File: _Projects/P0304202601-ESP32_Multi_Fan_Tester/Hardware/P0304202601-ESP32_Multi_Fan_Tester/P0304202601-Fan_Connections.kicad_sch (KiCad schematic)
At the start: 1 part, among them CN1 KHS4B-PH-SM4-TB(LF)(SN)

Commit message: Added new content from recent stream.
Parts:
- added CN4: KTBL002B-350-04GR-2OR, CONNECTORS:KTBTBL002B35004GR2OR, symbol CONNECTORS:KTBL002B-350-04GR-2OR
- added CN5: KH470533000, CONNECTORS:KH470533000, symbol CONNECTORS:KH470533000
- added J1, J2, J3: KH22-28-5021, CONNECTORS:2x1HDR2.54mm, symbol CONNECTORS:KH22-28-5021
- added R2: RC06031K0075AAA, COMPONENTS:RES-0603, symbol COMPONENTS:RC06031K0075AAA
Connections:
- new net +3.3V: R2.1
- new net FAN_PWM: CN5.4
- new net FAN_TACH: CN5.3, R2.2
- new net FAN_VCC: CN5.2
- new net GND: CN5.1
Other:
- moved on the sheet: CN1

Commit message: Added updated content that I keep forgetting to do.
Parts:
- added D3, D4, D5: DLQ62702P5179, COMPONENTS:LED-0805, symbol COMPONENTS:DLQ62702P5179
- added Q1, Q2, Q3: SSM3K2615R,LF, COMPONENTS:SOT-23F-3, symbol COMPONENTS:QSSM3K2615R,LF
- added R11: 100Ω, COMPONENTS:RES-0603, symbol COMPONENTS:RC0603100RAAD07500
- added R12: RC060310K2075AAA, COMPONENTS:RES-0603, symbol COMPONENTS:RC060310K2075AAA
- added R4: RC0603330075AAA, COMPONENTS:RES-0603, symbol COMPONENTS:RC0603330075AAA
- added R5: RC0603510075AAA, COMPONENTS:RES-0603, symbol COMPONENTS:RC0603510075AAA
- added R6: RC06031K0075AAA, COMPONENTS:RES-0603, symbol COMPONENTS:RC06031K0075AAA
- added TP3, TP4, TP5, TP6: TP5010, CONNECTORS:5010, symbol CONNECTORS:TP5010
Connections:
- net +12V: now also Q3.3 (D)
- net +3.3V: now also Q1.3 (D)
- net +5V: now also Q2.3 (D)
- net FAN_PWM: now also CN1.3, CN4.3, TP6.1
- net FAN_TACH: now also CN1.2, CN4.2, TP3.1
- net FAN_VCC: now also CN1.1, CN4.1, J1.2, J2.2, J3.2, R4.1, R5.1, R6.1
- net GND: now also CN1.4, CN4.4, D3.1 (K), D4.1 (K), D5.1 (K), R12.2, TP5.1
- net at J2.1: now also Q2.2 (S)
- net at J3.1: now also Q3.2 (S)
- net at J1.1: now also Q1.2 (S)
- new net: D5.2 (A), R6.2
- new net: D3.2 (A), R4.2
- new net: D4.2 (A), R5.2
- new net FAN_PWR_CNTROL: R11.1, R12.1, TP4.1
- new net PWR_CNTRL: Q1.1 (G), Q2.1 (G), Q3.1 (G), R11.2
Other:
- moved on the sheet: CN1, CN4, CN5, J1, J2, J3, R2

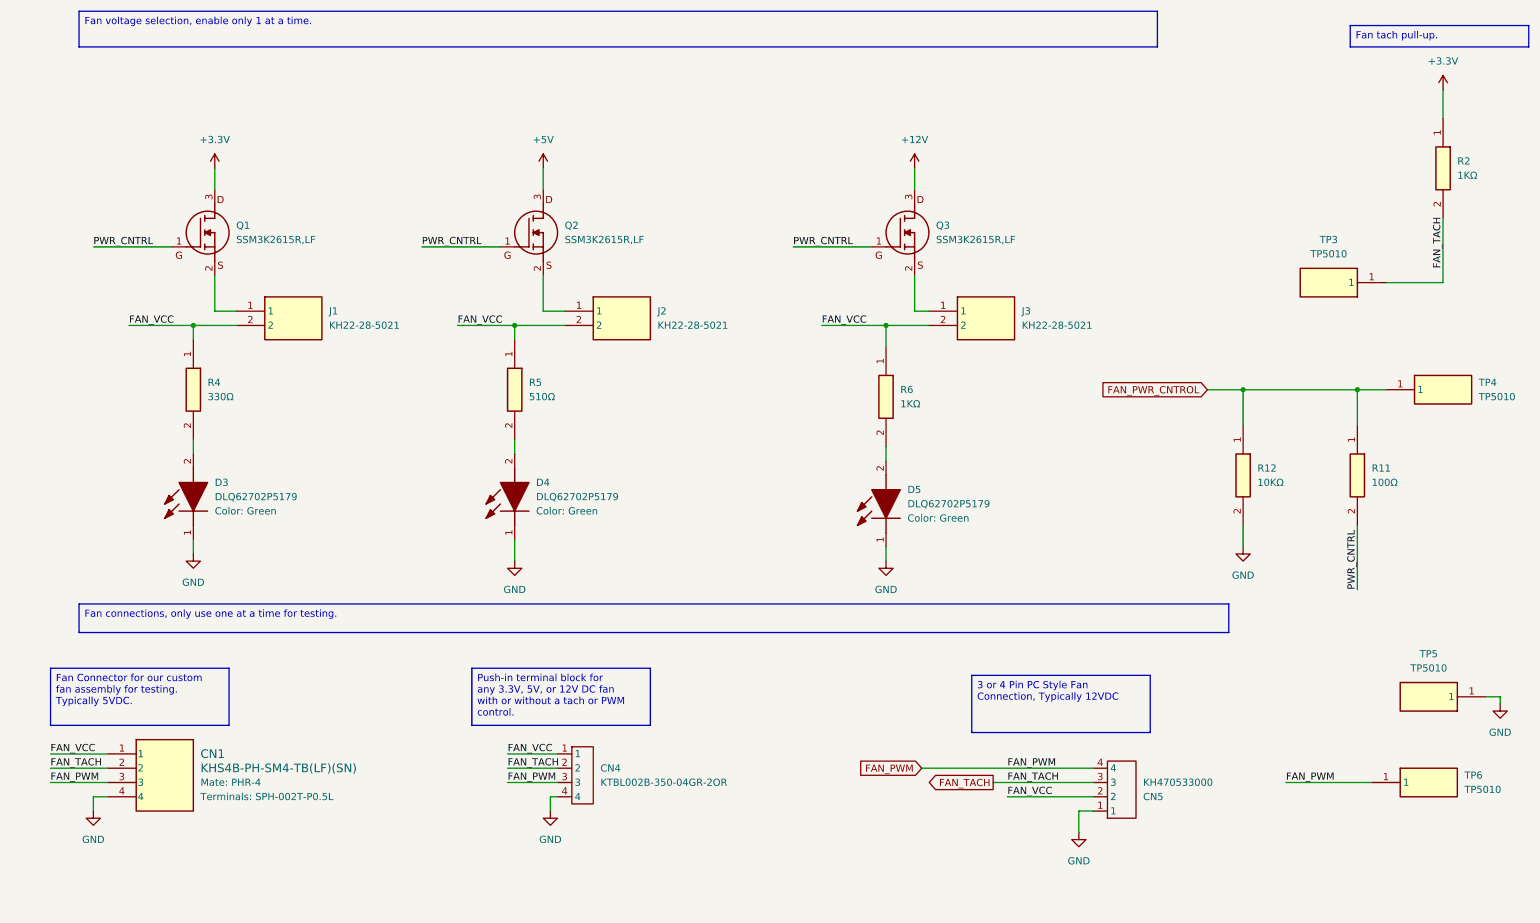
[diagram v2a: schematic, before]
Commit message: Updated files from video stream.
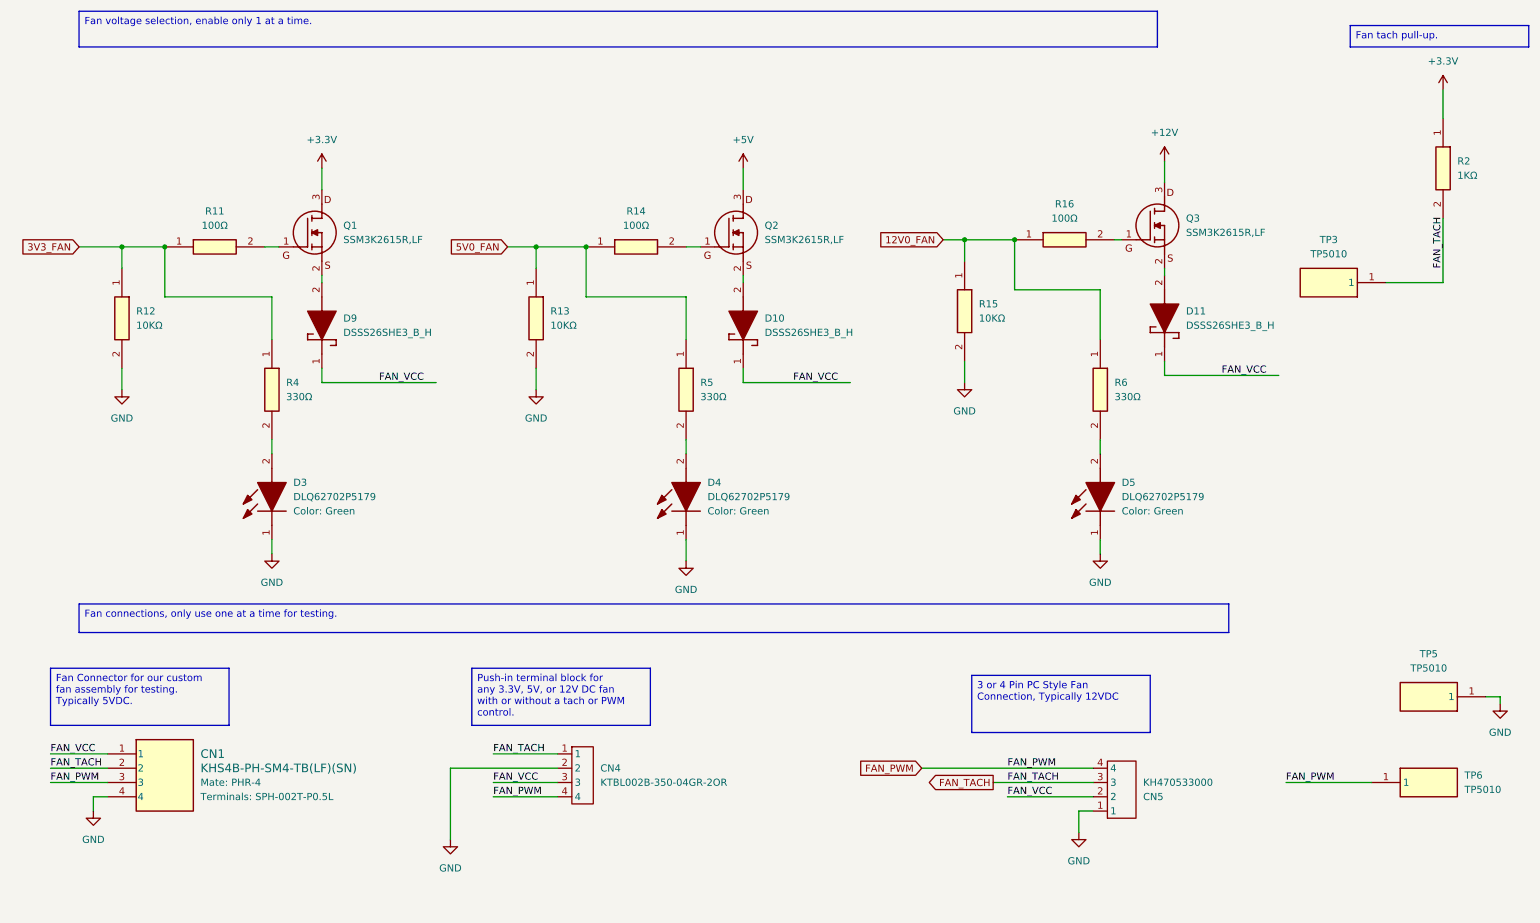
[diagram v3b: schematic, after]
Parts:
- removed J1, J2, J3: KH22-28-5021, CONNECTORS:2x1HDR2.54mm, symbol CONNECTORS:KH22-28-5021
- removed R5: RC0603510075AAA, COMPONENTS:RES-0603, symbol COMPONENTS:RC0603510075AAA
- removed R6: RC06031K0075AAA, COMPONENTS:RES-0603, symbol COMPONENTS:RC06031K0075AAA
- removed TP4: TP5010, CONNECTORS:5010, symbol CONNECTORS:TP5010
- added D10, D11, D9: DSSS26SHE3_B_H, COMPONENTS:SMA, symbol COMPONENTS:DSSS26SHE3_B_H
- added R13, R15: RC060310K2075AAA, COMPONENTS:RES-0603, symbol COMPONENTS:RC060310K2075AAA
- added R14, R16: 100Ω, COMPONENTS:RES-0603, symbol COMPONENTS:RC0603100RAAD07500
- added R5, R6: RC0603330075AAA, COMPONENTS:RES-0603, symbol COMPONENTS:RC0603330075AAA
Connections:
- net FAN_PWM: now also CN4.4; no longer CN4.3
- net FAN_TACH: now also CN4.1; no longer CN4.2
- net FAN_VCC: now also CN4.3, D10.1 (K), D11.1 (K), D9.1 (K); no longer CN4.1, R4.1
- net GND: now also CN4.2, R13.2, R15.2; no longer CN4.4
- net at Q2.2 (S): now also D10.2 (A)
- net at D5.2 (A): now also R6.2
- net at Q3.2 (S): now also D11.2 (A)
- net at Q1.2 (S): now also D9.2 (A)
- net at D4.2 (A): now also R5.2
- net FAN_PWR_CNTROL renamed 3V3_FAN
- net 3V3_FAN: now also R4.1
- net PWR_CNTRL: no longer names the net of Q1.1 (G), R11.2
- net PWR_CNTRL: no longer Q2.1 (G), Q3.1 (G)
- new net: Q2.1 (G), R14.2
- new net: Q3.1 (G), R16.2
- new net 12V0_FAN: R15.1, R16.1, R6.1
- new net 5V0_FAN: R13.1, R14.1, R5.1
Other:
- moved on the sheet: D3, D4, D5, Q1, Q2, Q3, R11, R12, R4
